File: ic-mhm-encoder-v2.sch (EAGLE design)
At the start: 21 parts, among them J1 5040500291, J2 5040501191, M1 BSS670S2LH6327XTSA1, U1 24LC16BT-I/MC, U2 D5V0F4U6S-7, U3 D5V0F4U6S-7, U4 D5V0F4U6S-7, U6 UA9638CDR

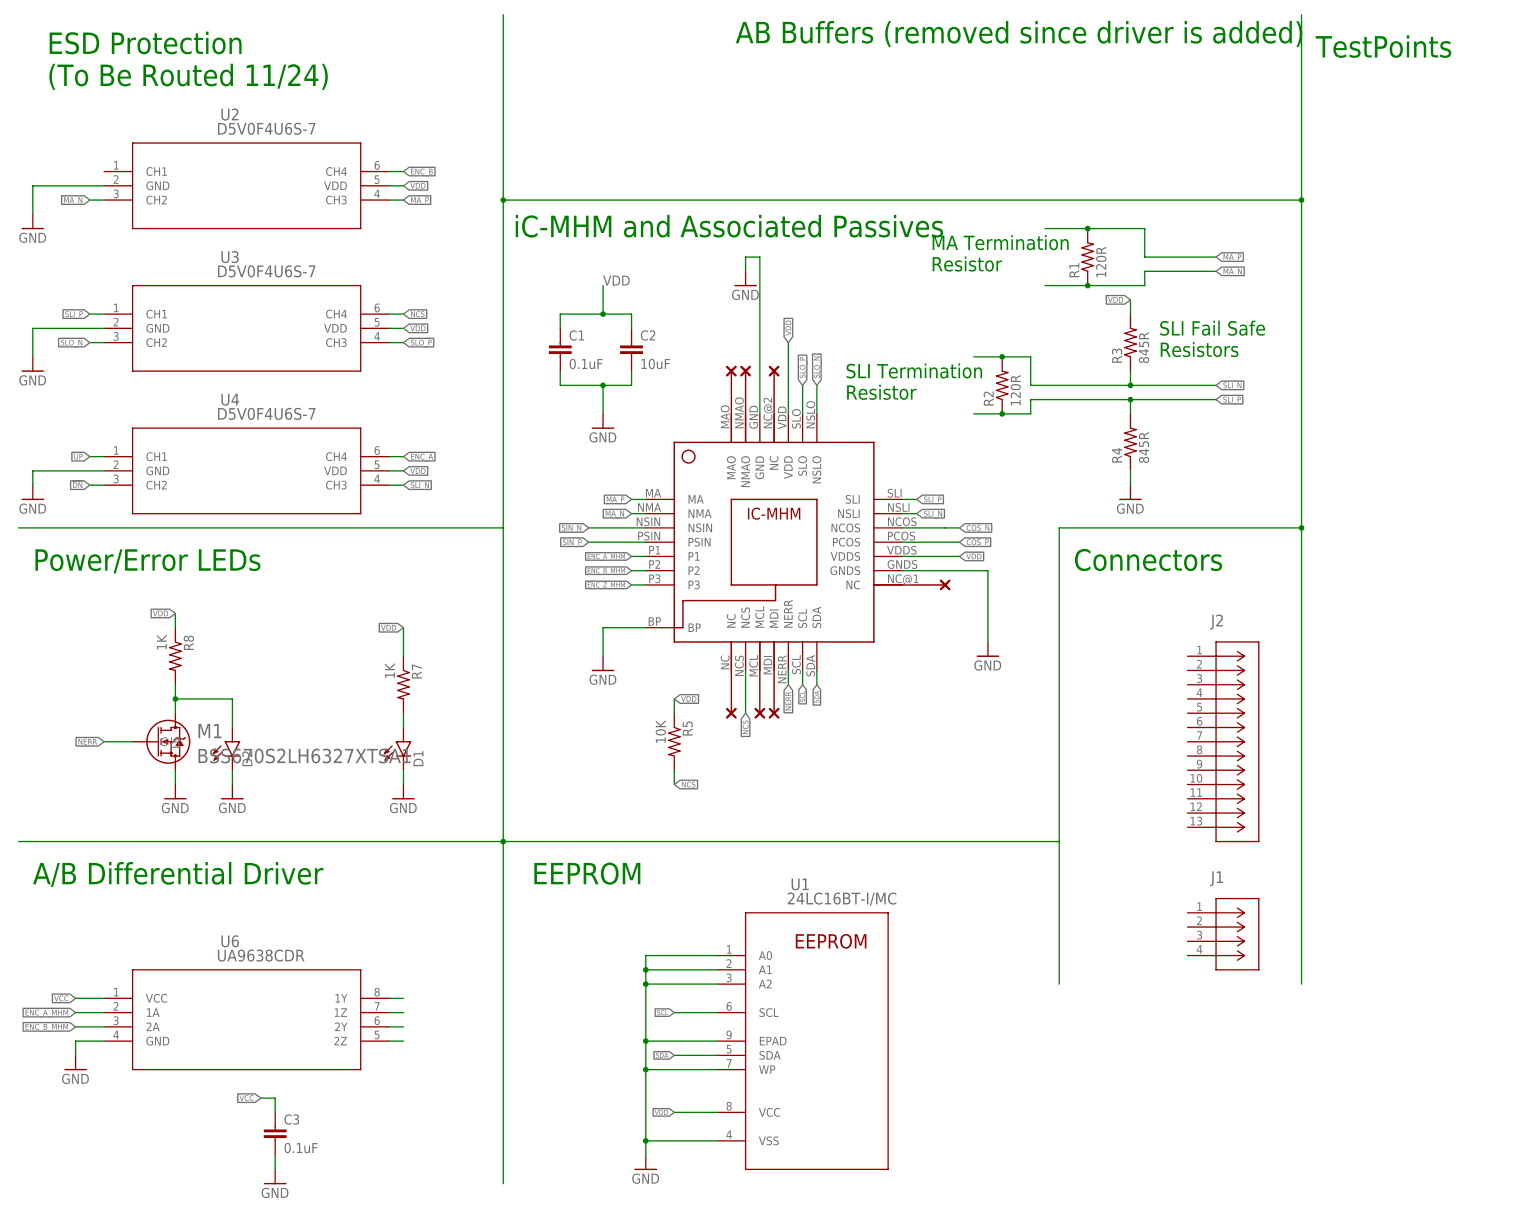
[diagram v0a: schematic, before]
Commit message: Finished routing of v2 pcb, ready for design review
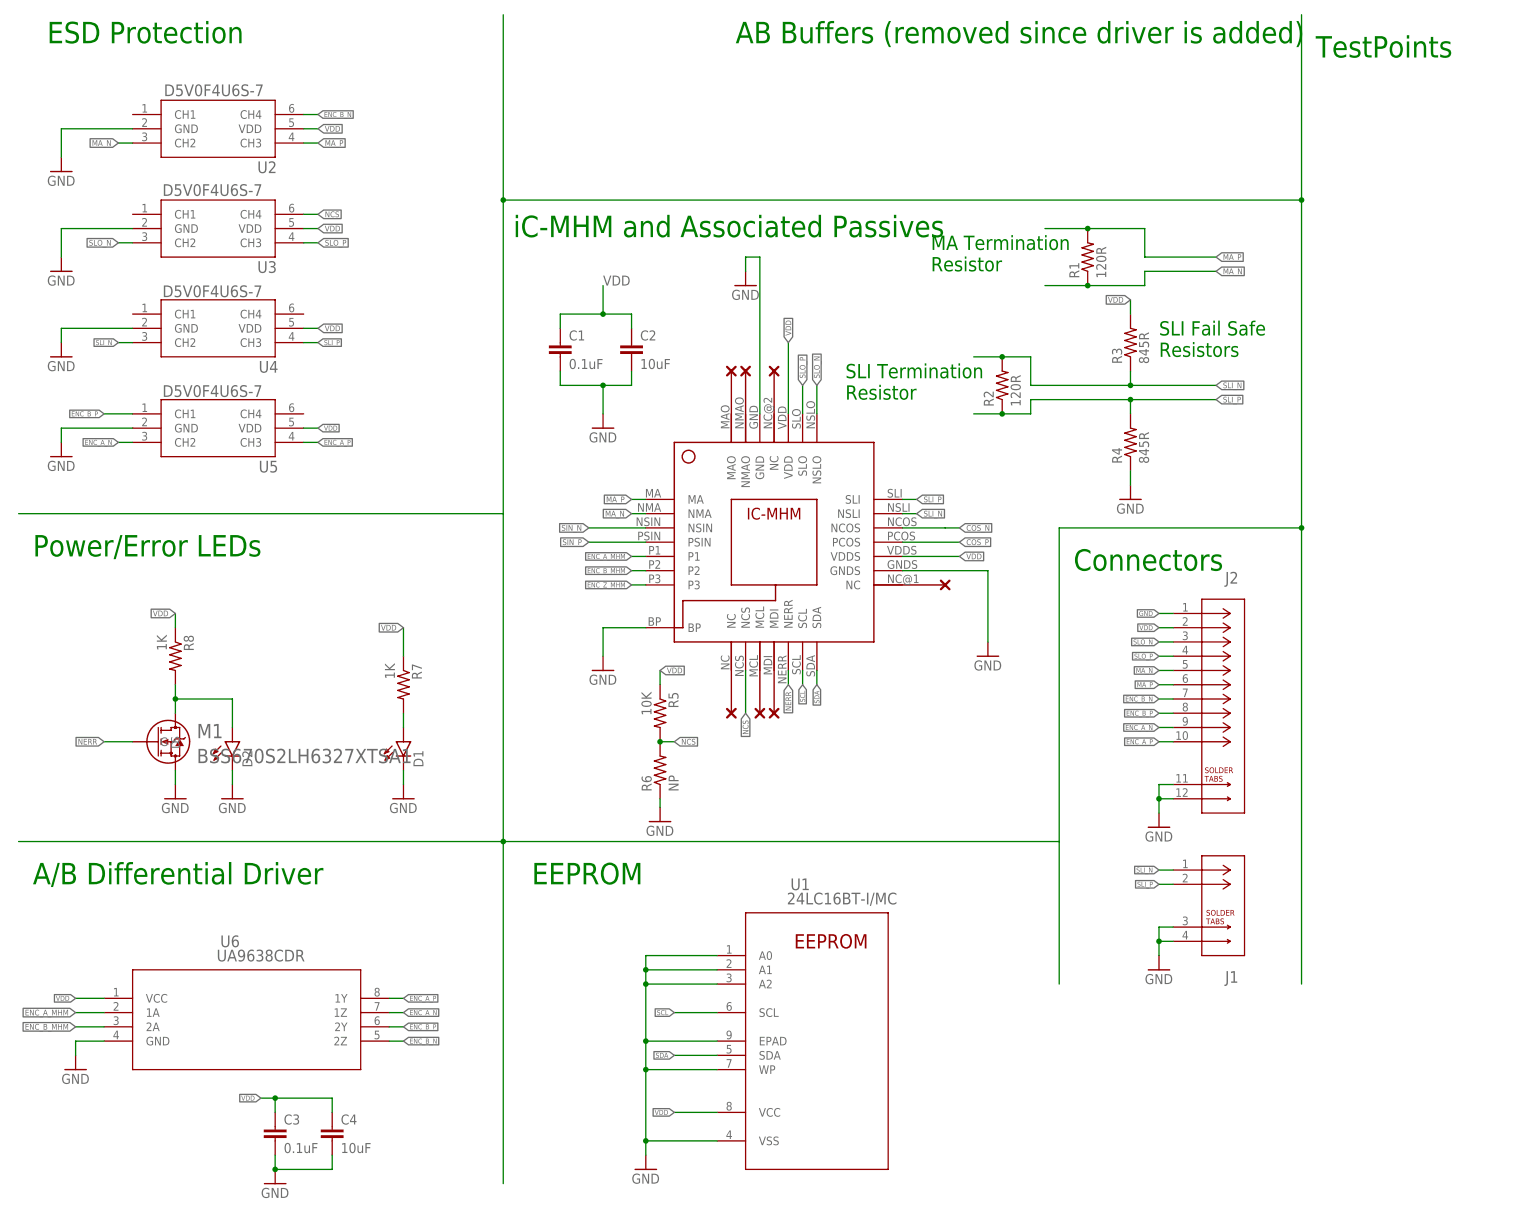
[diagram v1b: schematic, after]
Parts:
- added C4: 10uF, rcl:C-EUC0603
- added R6: NP, rcl:R-US_R0603
- added U5: D5V0F4U6S-7, ic-mhm:D5V0F4U6S-7
- C2: device rcl:C-EUC0805 -> rcl:C-EUC0603
- J1: value 5040500291 -> 2023960207; device ic-mhm:5040500291 -> ic-mhm:2023960207
- J2: value 5040501191 -> 2023961007; device ic-mhm:5040501191 -> ic-mhm:2023961007
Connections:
- removed net !DN: U4.CH2
- removed net !UP: U4.CH1
- removed net ENC_A: U4.CH4
- removed net ENC_B: U2.CH4
- removed net N$3: U6.1Y
- removed net N$7: U6.1Z
- removed net N$8: U6.2Y
- removed net N$9: U6.2Z
- removed net VCC: C3.1, U6.VCC
- new net ENC_A_N: J2.9, U5.CH2, U6.1Z
- new net ENC_A_P: J2.10, U5.CH3, U6.1Y
- new net ENC_B_N: J2.7, U2.CH4, U6.2Z
- new net ENC_B_P: J2.8, U5.CH1, U6.2Y
- net GND: now also C4.2, J1.3, J1.4, J2.1, J2.11, J2.12, R6.1, U5.GND
- net MA_N: now also J2.5
- net MA_P: now also J2.6
- net NCS: now also R6.2
- net SLI_N: now also J1.1, U4.CH2; no longer U4.CH3
- net SLI_P: now also J1.2, U4.CH3; no longer U3.CH1
- net SLO_N: now also J2.3
- net SLO_P: now also J2.4
- net VDD: now also C3.1, C4.1, J2.2, U5.VDD, U6.VCC
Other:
- note added: "ESD Protection"
- note removed: "ESD Protection (To Be Routed 11/24)"
- moved on the sheet: R5, U2, U3, U4

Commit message: added mfg and assembly files for v2
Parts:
- removed R6: NP, rcl:R-US_R0603
- added FID1, FID2, FID3, FID4, FID5, FID6, FID7, FID8: FIDUCIAL_1MM, microbuilder:FIDUCIAL_1MM
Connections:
- net GND: no longer R6.1
- net NCS: no longer R6.2
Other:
- note added: "Bottom"
- note added: "Fiducials"
- note added: "Top"
- note removed: "AB Buffers (removed since driver is added)"
- note removed: "TestPoints"
